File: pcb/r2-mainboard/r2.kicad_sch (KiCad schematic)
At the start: 0 parts

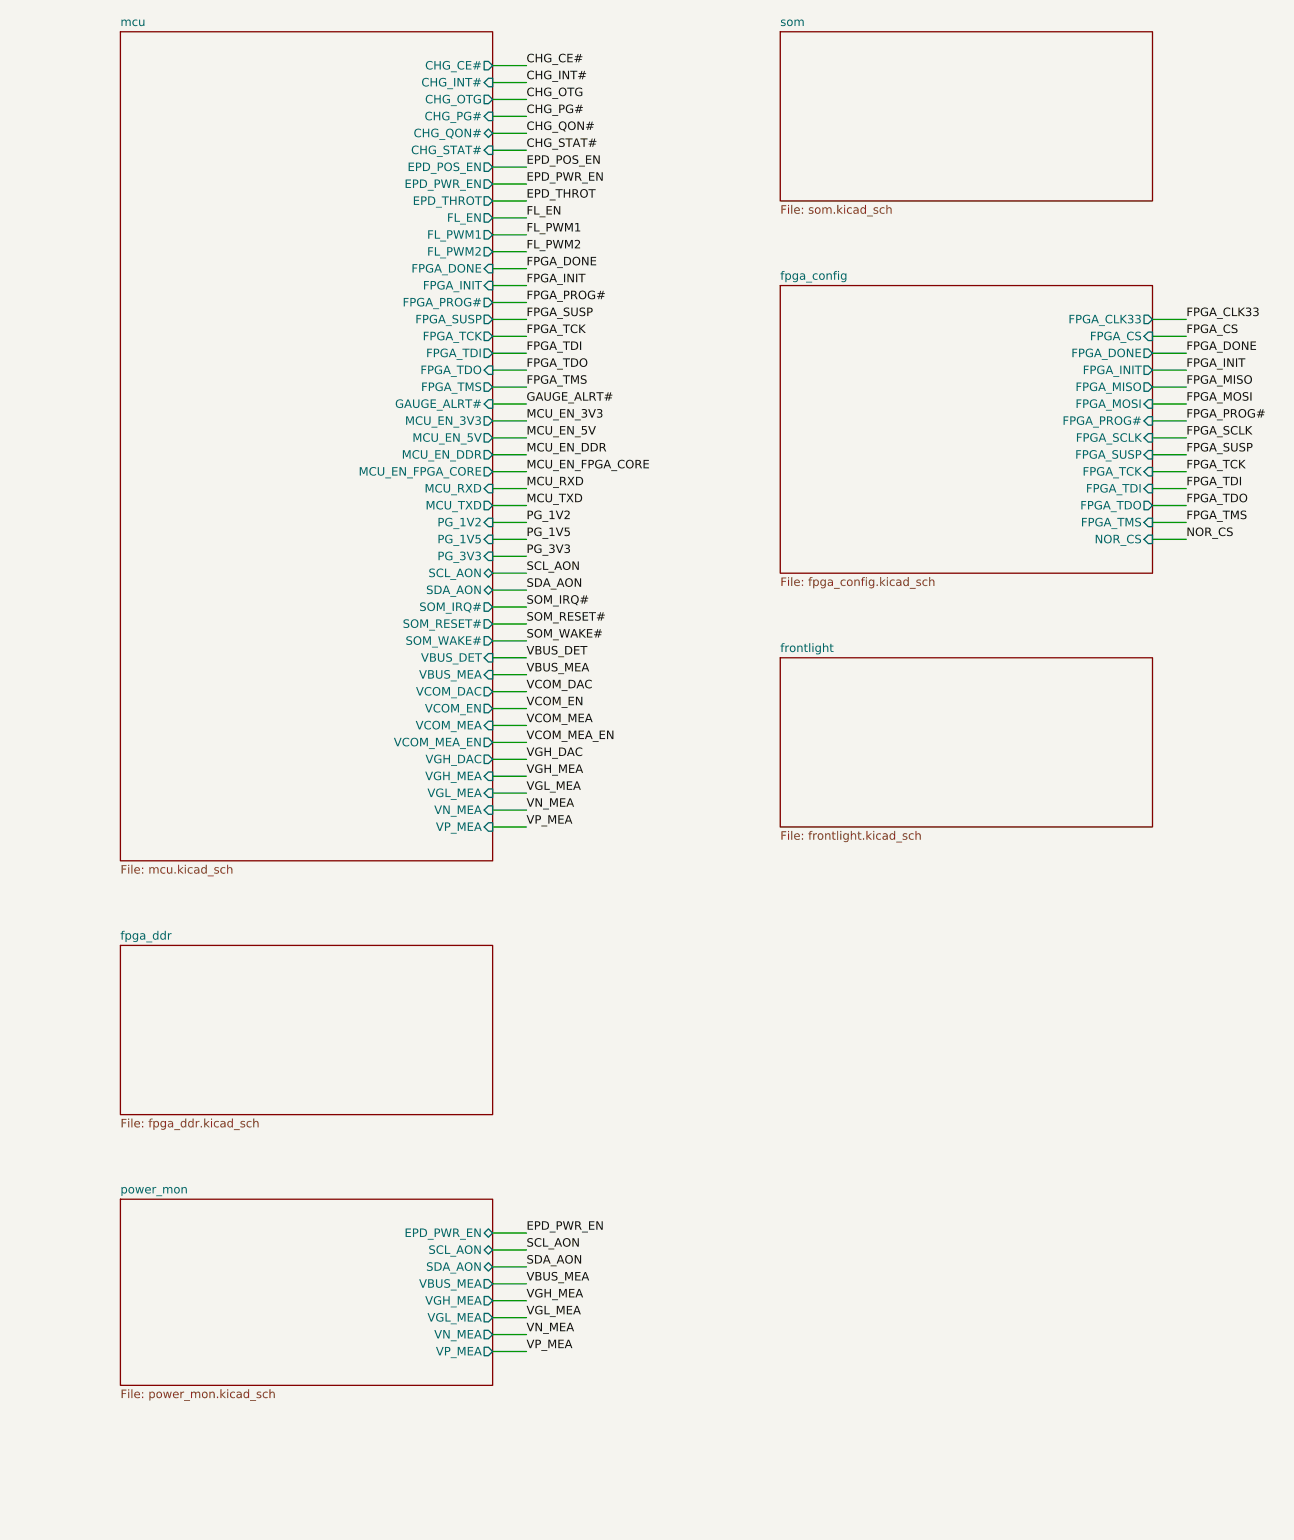
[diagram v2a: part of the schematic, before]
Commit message: R2: WP8 -- som drawn; the hierarchy has no dangling interfaces left
tools/gen_som.py draws som.kicad_sch: PCM-071 units 1, 3 and 4 (unit 2, the DPI
link, is on dpi_in), the microSD on MMC1, and the last 12 interface nets.
patch_mcu_pg_som.py claims PC8 for PG_SOM at the MCU end. Root state: 100 names,
100 joined, 0 one-sided -- wire_root.py's DANGLING_OK is now empty, so anything
one-sided from here is a genuinely forgotten interface rather than pending work.

TWO PINS CHOSEN THAT docs/som.md HAD LEFT OPEN. PHYTEC's manual never uses the
word "wake" -- it is not in the document -- so the answer came from TI's AM62x
datasheet (SPRSP58C) instead. Cross-referencing every X1 pin's AM62x ball
against the datasheet's pin-mux table shows exactly 22 X1 pins reach an
MCU_GPIO0_*, i.e. a GPIO in the MCU always-on domain that survives DeepSleep;
the other ~170 signal pins are MAIN-domain and could not wake the module
whatever firmware did. Among those 22, CAN is the one function a reader can
never want:

    SOM_WAKE#  A58  X_MCU_MCAN0_RX  ball B3  = MCU_GPIO0_14
    SOM_IRQ#   A57  X_MCU_MCAN0_TX  ball D6  = MCU_GPIO0_13

Confirm at bring-up, and the doc says so: "Partial IO" is a different low-power
mode from DeepSleep, and PHYTEC demonstrated GPIO wake from Suspend-to-RAM
without naming the pin. The domain is proven; the specific pin is not. Moving
to another of the 22 is a one-net edit, which is why the choice came from that
set. A59/A60 are the next candidates and sit on the same symbol unit.

A SECOND SILENT SHORT, and the netlist caught it after the render did not. The
first fix for a +VBUS power symbol colliding with the USB labels dropped a
vertical wire 10.16 mm to clear them -- and that wire ran through the label
anchors four rows below, shorting SOM_IRQ# and SOM_WAKE# to +VBUS. Both nets
simply vanished from the netlist. ERC reported nothing, because nothing was
illegal. Fixed by giving the symbol room horizontally instead, on a row where
it cannot touch anything.
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
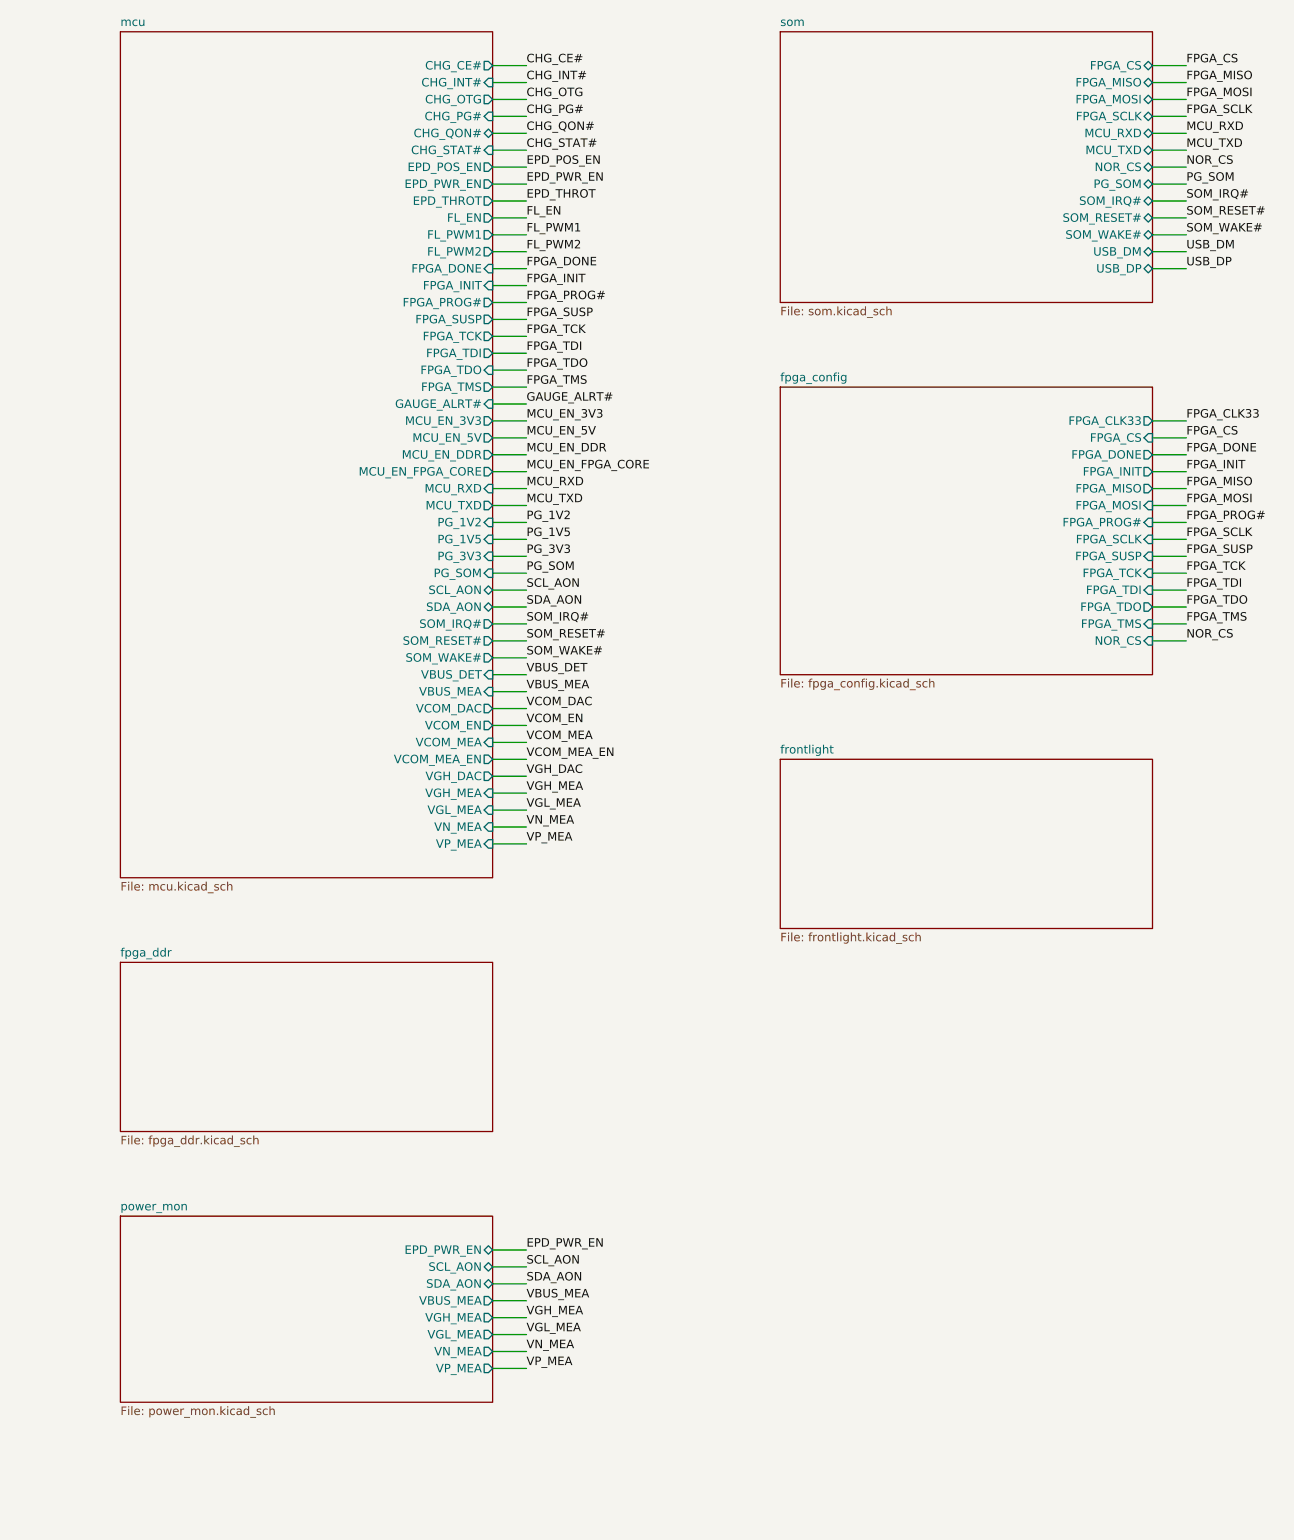
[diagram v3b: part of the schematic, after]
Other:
- sheet mcu ports: added PG_SOM; removed none
- sheet som ports: added FPGA_CS, FPGA_MISO, FPGA_MOSI, FPGA_SCLK, MCU_RXD, MCU_TXD, NOR_CS, PG_SOM, SOM_IRQ#, SOM_RESET#, SOM_WAKE#, USB_DM, USB_DP; removed none

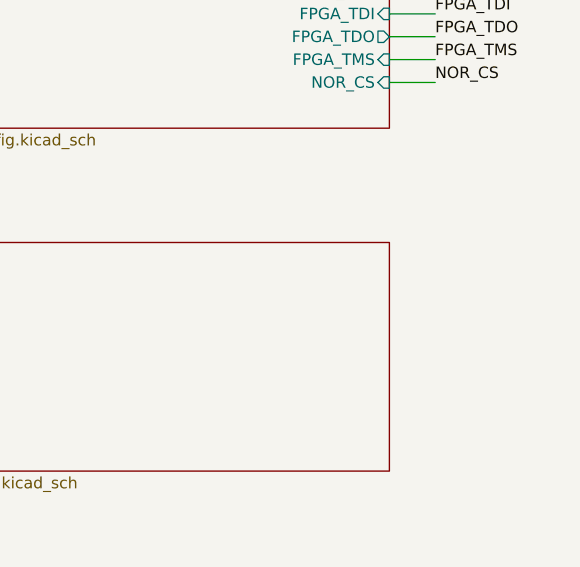
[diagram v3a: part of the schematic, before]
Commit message: R2: WP6a -- frontlight drawn, and it closes a hole rather than adding a feature
The netlist said it plainly before this sheet existed:

    +5V2_FL    C147.1  J6.44  J6.7      <- three loads, no source
    +VSYS_FL   R72.1   U22.1            <- a shunt into an ammeter, going nowhere

R1 fed +5V2_FL from +5V_DCDC through shunt R72, so the panel saw about 4.99 V.
WP2 moved the frontlight to the cell -- power_mon's U22 ch3 became
+VSYS -> +VSYS_FL -- and left the converter to WP6. Until now the rail was
orphaned at one end and the shunt dead-ended at the other. Verified against R1
by exporting its netlist from a copy in /tmp; pcb/mainboard/ never touched.

U53 is a second TPS61022, same topology as U12 and deliberately the same
feedback values: 732k/100k = 4.992 V. That adds no new passive line items, and
one DFE322512F now covers L10, L12, L13 and L33.

Why ~5.0 V and not 5.2: the net name was already wrong in R1, where it came off
a 5.0 V rail. epd-port.md 7 left "confirm or rename" to WP6. Confirmed at R1's
proven value and the name kept -- the panel-side circuit is unknown because the
panel is, so matching what R1 actually delivered is the conservative choice, and
renaming would touch frozen epd.kicad_sch for a cosmetic gain. If a chosen panel
wants a different string voltage it is two resistors.

The architecture is R1's and is not obvious, so it is written down: there is no
LED driver on this board and there was none on R1. The board supplies a voltage
rail plus FL_EN/FL_PWM1/FL_PWM2 to J6, and the panel's tail regulates the LED
current and does the dimming. FL_EN now has four nodes -- MCU, J6, U53.EN and
its pull-down -- because one signal means "frontlight on" and there is no case
where the boost and the panel side should disagree.

Sized deliberately oversized: a 3 A part for ~100 mA. The alternative is a new
IC, footprint, inductor and stock check to save a few hundred uA on a rail that
is off whenever the light is off. TPS61022 draws 27 uA + 0.9 uA running, 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
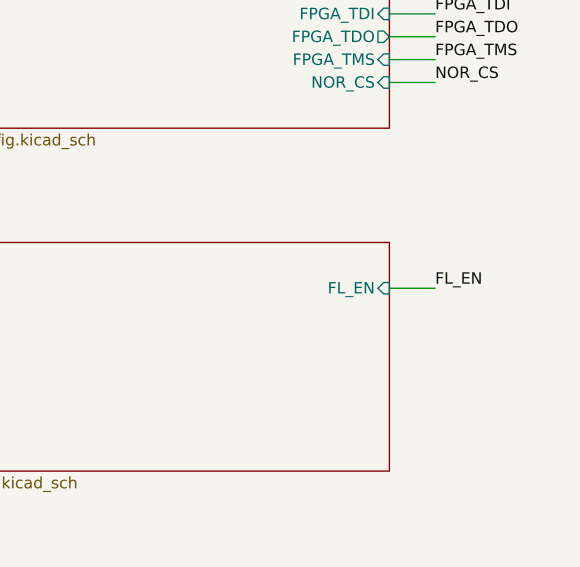
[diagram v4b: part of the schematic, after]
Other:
- sheet frontlight ports: added FL_EN; removed none
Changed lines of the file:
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@@
 			)
 		)
+		(pin "FL_EN" input
+			(at 375.92 144.78 0)
+			(effects
+				(font
+					(size 1.27 1.27)
+				)
+				(justify right)
+			)
+		)
 		(instances
 			(project "r2"
@@
 		(effects
 			(font
+				(size 1.27 1.27)
+			)
+			(justify left bottom)
+		)
+	)
+	(wire
+		(pts
+			(xy 375.92 144.78) (xy 381.0 144.78)
+		)
+		(stroke
+			(width 0)
+			(type default)
+		)
+	)
+	(label "FL_EN"
+		(at 381.0 144.78 0)
+		(effects
+			(font
